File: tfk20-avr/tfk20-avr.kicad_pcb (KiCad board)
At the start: 4 copper layers, 76.2 x 115.5 mm, 123 parts, among them J1 USB_C_Receptacle_USB2.0, J2 AVR-ISP-6, SW1 Reset, U1 ATmega32U4-AU, U2 IS31FL3733-TQ, Y1 16MHz

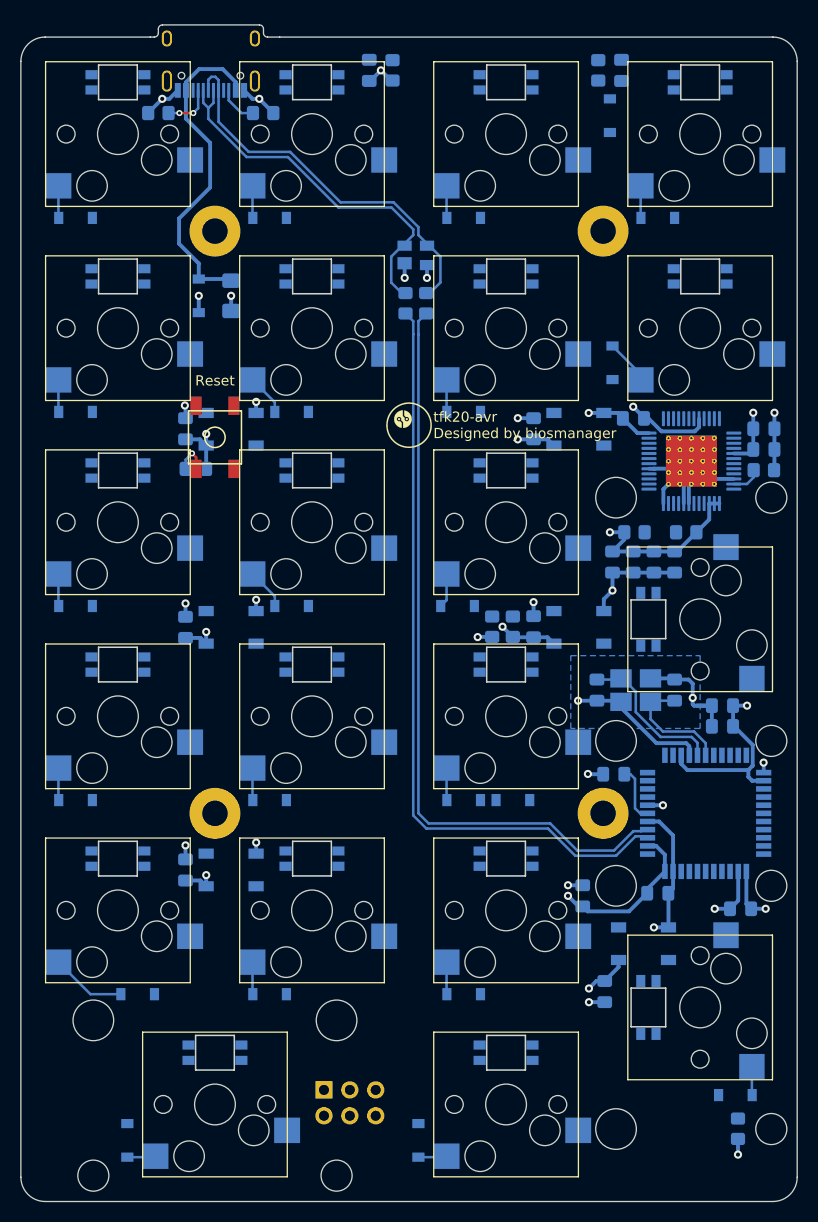
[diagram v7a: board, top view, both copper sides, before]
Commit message: Route columns
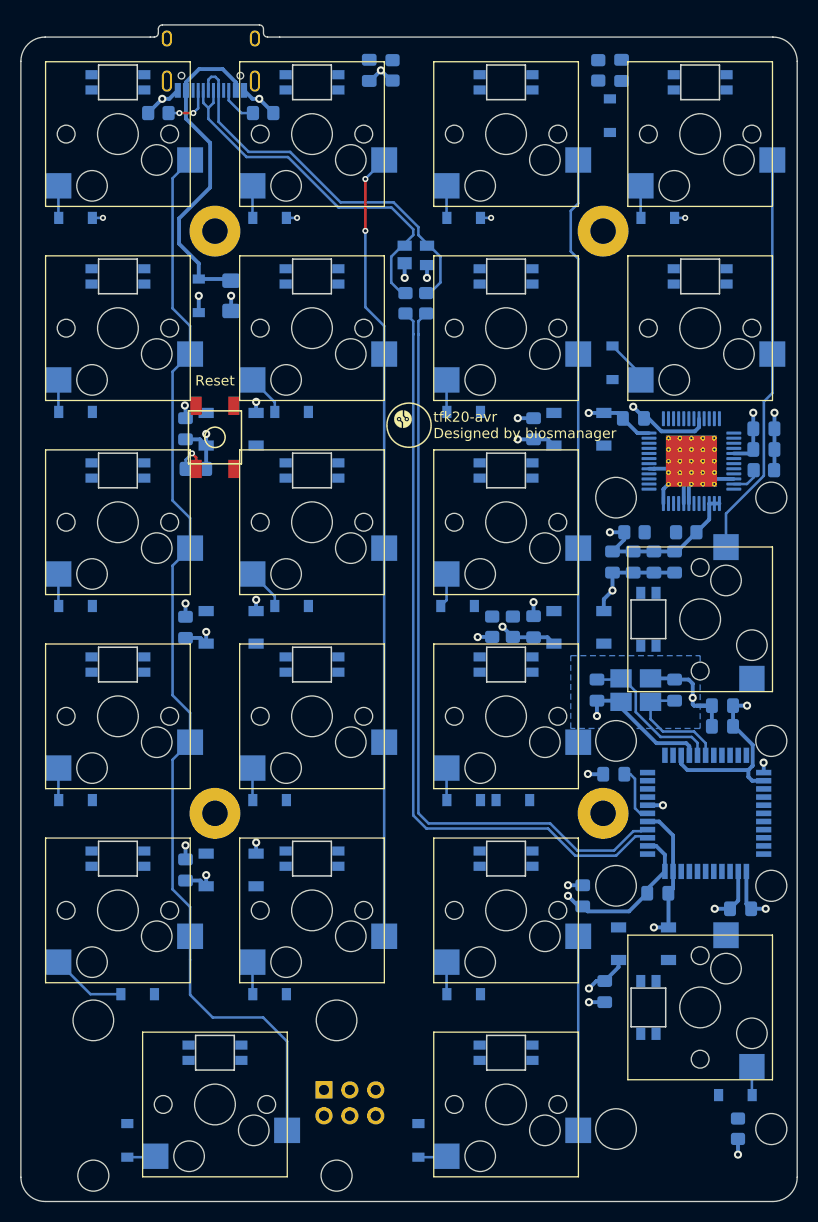
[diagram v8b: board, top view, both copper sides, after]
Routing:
- net /COL_0: track 0.00 -> 107.8 mm
- net /COL_2: track 0.00 -> 79.2 mm
- net /COL_1: track 0.00 -> 77.7 mm, vias 0 -> 2
- net /COL_3: track 0.00 -> 39.9 mm
- net /ROW_0: track 0.00 -> 4.17 mm, vias 0 -> 4
- added copper zone on PWR, net +5V
- removed copper zone on POWER, net +5V
